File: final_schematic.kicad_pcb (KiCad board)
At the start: 2 copper layers, 0 parts

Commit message: Component Check Passed
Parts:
- added C1: 1uF, Capacitor_SMD:C_0603_1608Metric_Pad1.08x0.95mm_HandSolder, F.Cu at (-15.2, 27.3)
- added C10: 0.1uF, Capacitor_SMD:C_0402_1005Metric_Pad0.74x0.62mm_HandSolder, F.Cu at (-14.5, 115.2)
- added C11: 0.1uF, Capacitor_SMD:C_0402_1005Metric_Pad0.74x0.62mm_HandSolder, F.Cu at (-13.8, 125.4)
- added C12: 1uF, Capacitor_SMD:C_0603_1608Metric_Pad1.08x0.95mm_HandSolder, F.Cu at (-13.4, 135.0)
- added C13: 0.1uF, Capacitor_SMD:C_0402_1005Metric_Pad0.74x0.62mm_HandSolder, F.Cu at (-13.7, 145.2)
- added C14: 10uF, Capacitor_SMD:C_0603_1608Metric_Pad1.08x0.95mm_HandSolder, F.Cu at (-13.0, 155.1)
- added C15: 0.1uF, Capacitor_SMD:C_0402_1005Metric_Pad0.74x0.62mm_HandSolder, F.Cu at (-13.0, 164.9)
- added C16: 0.12uF, Capacitor_SMD:C_0603_1608Metric_Pad1.08x0.95mm_HandSolder, F.Cu at (-12.4, 175.1)
- added C17: 0.0068uF, Capacitor_SMD:C_0603_1608Metric_Pad1.08x0.95mm_HandSolder, F.Cu at (-11.4, 185.0)
- added C18: 0.1uF, Capacitor_SMD:C_0402_1005Metric_Pad0.74x0.62mm_HandSolder, F.Cu at (-12.9, 195.6)
- added C2: 1uF, Capacitor_SMD:C_0603_1608Metric_Pad1.08x0.95mm_HandSolder, F.Cu at (-15.3, 37.5)
- added C3: 1uF, Capacitor_SMD:C_0603_1608Metric_Pad1.08x0.95mm_HandSolder, F.Cu at (-15.4, 46.8)
- added C4: 1uF, Capacitor_SMD:C_0603_1608Metric_Pad1.08x0.95mm_HandSolder, F.Cu at (-15.2, 55.3)
- added C5: 0.1uF, Capacitor_SMD:C_0402_1005Metric_Pad0.74x0.62mm_HandSolder, F.Cu at (-15.3, 64.5)
- added C6: 0.1uF, Capacitor_SMD:C_0402_1005Metric_Pad0.74x0.62mm_HandSolder, F.Cu at (-15.2, 74.0)
- added C7: 0.1uF, Capacitor_SMD:C_0402_1005Metric_Pad0.74x0.62mm_HandSolder, F.Cu at (-15.1, 84.5)
- added C8: 0.1uF, Capacitor_SMD:C_0402_1005Metric_Pad0.74x0.62mm_HandSolder, F.Cu at (-14.9, 94.6)
- added C9: 0.1uF, Capacitor_SMD:C_0402_1005Metric_Pad0.74x0.62mm_HandSolder, F.Cu at (-14.7, 105.1)
- added D1: LED_HEARTBEAT_R1, Diode_SMD:D_0603_1608Metric_Pad1.05x0.95mm_HandSolder, F.Cu at (21.6, 16.5)
- added D2: LED_TRANSMIT_G1, Diode_SMD:D_0201_0603Metric_Pad0.64x0.40mm_HandSolder, F.Cu at (57.0, 17.2)
- added J1: BB_COM_Conn_01x04_Male, Connector_PinHeader_1.00mm:PinHeader_1x04_P1.00mm_Vertical, F.Cu at (113.6, 129.6)
- added J2: BB_CTRL_Conn_01x02_Male, Connector_PinHeader_1.00mm:PinHeader_1x02_P1.00mm_Vertical, F.Cu at (113.8, 151.0)
- added J3: BB_ON/OFF_Conn_01x04_Male, Connector_PinHeader_1.00mm:PinHeader_1x01_P1.00mm_Vertical, F.Cu at (112.3, 114.0)
- added J4: BOOT0_Conn_Male, Connector_PinHeader_1.00mm:PinHeader_1x01_P1.00mm_Vertical, F.Cu at (113.7, 144.8)
- added J5: OLED_SPI_Conn_01x04_Male, Connector_PinHeader_1.00mm:PinHeader_1x06_P1.00mm_Vertical, F.Cu at (112.5, 118.7)
- added J6: OLED_EN_Conn_01x02_Male, Connector_PinHeader_1.00mm:PinHeader_1x01_P1.00mm_Vertical, F.Cu at (113.4, 138.0)
- added J7: Conn_ARM_JTAG_SWD_10, Connector_PinHeader_1.27mm:PinHeader_2x05_P1.27mm_Vertical_SMD, F.Cu at (219.7, 68.6)
- added J8: GPS_COAX, Connector_Coaxial:U.FL_Molex_MCRF_73412-0110_Vertical, F.Cu at (240.0, 118.3)
- added LoRa_CON_Coaxial1: LoRa_Conn_Coaxial, Connector_Coaxial:U.FL_Molex_MCRF_73412-0110_Vertical, F.Cu at (244.0, 151.1)
- added R1: 48, Resistor_SMD:R_0603_1608Metric_Pad0.98x0.95mm_HandSolder, F.Cu at (-2.32, 39.5)
- added R10: 1k, Resistor_SMD:R_0402_1005Metric_Pad0.72x0.64mm_HandSolder, F.Cu at (-1.38, 106.3)
- added R2: 48, Resistor_SMD:R_0603_1608Metric_Pad0.98x0.95mm_HandSolder, F.Cu at (-2.32, 45.9)
- added R3: 10k, Resistor_SMD:R_0603_1608Metric_Pad0.98x0.95mm_HandSolder, F.Cu at (-2.45, 51.6)
- added R4: 10k, Resistor_SMD:R_0603_1608Metric_Pad0.98x0.95mm_HandSolder, F.Cu at (-2.50, 57.7)
- added R5: 10k, Resistor_SMD:R_0603_1608Metric_Pad0.98x0.95mm_HandSolder, F.Cu at (-2.51, 65.7)
- added R6: 510, Resistor_SMD:R_0603_1608Metric_Pad0.98x0.95mm_HandSolder, F.Cu at (-2.21, 73.5)
- added R7: 2.2k, Resistor_SMD:R_0603_1608Metric_Pad0.98x0.95mm_HandSolder, F.Cu at (-2.00, 81.1)
- added R8: 2.2k, Resistor_SMD:R_0603_1608Metric_Pad0.98x0.95mm_HandSolder, F.Cu at (-1.80, 89.3)
- added R9: 10k, Resistor_SMD:R_0603_1608Metric_Pad0.98x0.95mm_HandSolder, F.Cu at (-1.15, 101.0)
- added RED1: LED_GPS_R, Diode_SMD:D_0603_1608Metric_Pad1.05x0.95mm_HandSolder, F.Cu at (240.0, 110.2)
- added Re1: 10k, Resistor_SMD:R_0603_1608Metric_Pad0.98x0.95mm_HandSolder, F.Cu at (-2.19, 33.9)
- added Rf1: 10k, Resistor_SMD:R_0603_1608Metric_Pad0.98x0.95mm_HandSolder, F.Cu at (-2.41, 27.5)
- added S1: ON/OFF-SWITCH, Button_Switch_SMD:SW_SP3T_PCM13, F.Cu at (40.6, 160.0)
- added SW1: SW_Push_SESS, Button_Switch_SMD:SW_SPDT_CK-JS102011SAQN, F.Cu at (38.8, 17.8)
- added SW2: SW_Push_RADIO, Button_Switch_SMD:SW_SPST_PTS645, F.Cu at (163.2, 147.2)
- added SW3: SW_Push_RST, Button_Switch_SMD:SW_SPST_PTS645, F.Cu at (80.0, 149.9)
- added U1: STM32L476VGTx, Package_QFP:LQFP-100_14x14mm_P0.5mm, F.Cu at (166.4, 105.4)
- added U2: MTK3339, footprint_lib:FGPMMOPA6H, F.Cu at (223.5, 113.0)
- added U3: RFM95W-868S2, RF_Module:HOPERF_RFM9XW_SMD, F.Cu at (224.8, 144.8)
- added U4: BNO055, Package_LGA:LGA-28_5.2x3.8mm_P0.5mm, F.Cu at (218.4, 90.2)

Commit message: IMU, LORA, and GPS organized
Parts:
- moved C15 259.0 mm to (235.6, 92.1), turned to 90 degrees
- moved C16 256.6 mm to (230.4, 92.2), turned to 90 degrees
- moved C14 255.8 mm to (242.5, 144.0), turned to 180 degrees
- moved C17 254.3 mm to (225.3, 92.1), turned to 90 degrees
- moved C18 253.1 mm to (220.2, 97.0)
- moved Rf1 222.6 mm to (211.2, 90.1), turned to 90 degrees
- moved Re1 221.7 mm to (211.0, 94.7), turned to 90 degrees
- moved C13 220.2 mm to (203.1, 106.2), turned to 180 degrees
- moved R10 204.5 mm to (203.0, 112.3), turned to 180 degrees
- moved RED1 30.3 mm to (209.7, 112.3)
- moved LoRa_CON_Coaxial1 1.13 mm to (243.4, 150.2)

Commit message: Components spacialy assocsiated
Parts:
- moved C12 218.1 mm to (204.2, 149.3), turned to 180 degrees
- moved R9 211.5 mm to (206.1, 143.3), turned to 180 degrees
- moved C1 196.0 mm to (146.1, 138.7), turned to 180 degrees
- moved C2 176.2 mm to (129.6, 137.7)
- moved SW1 168.8 mm to (146.9, 147.5), turned to 0 degrees
- moved R3 168.7 mm to (142.0, 138.7)
- moved C3 159.3 mm to (115.5, 137.6)
- moved C6 158.9 mm to (141.6, 100.2)
- moved C7 157.9 mm to (141.6, 104.4)
- moved C8 157.1 mm to (141.6, 108.3)
- moved C9 156.5 mm to (141.6, 112.1)
- moved C10 156.1 mm to (141.6, 116.1)
- moved C11 155.5 mm to (141.6, 120.1)
- moved R7 155.4 mm to (152.2, 100.2)
- moved R8 154.7 mm to (152.8, 95.9)
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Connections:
- C15 pad 1: GND -> 3V3
- C15 pad 2: 3V3 -> GND
- J1 pad 1: I2C2_SDA -> GND
- J1 pad 2: I2C2_SCL -> V_supply
- J1 pad 3: V_supply -> I2C2_SDA
- J1 pad 4: GND -> I2C2_SCL

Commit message: Pre AI Routing Backup
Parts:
- moved D2 81.3 mm to (178.5, 133.1), turned to 90 degrees
- moved R2 68.6 mm to (177.6, 136.2), turned to 90 degrees
- moved C12 57.0 mm to (170.5, 103.3)
- moved R9 57.0 mm to (172.4, 97.3)
- moved J5 57.0 mm to (177.5, 93.7)
- moved J6 57.0 mm to (177.4, 103.2)
- moved J7 48.9 mm to (105.1, 91.5)
- moved J8 30.8 mm to (180.3, 120.8)
- moved U2 28.1 mm to (166.6, 115.5)
- moved R10 27.6 mm to (146.2, 116.5)
- moved RED1 27.6 mm to (152.9, 116.5)
- moved R8 22.9 mm to (130.2, 92.1)
- moved U1 22.9 mm to (133.2, 108.8)
- moved C13 22.9 mm to (150.9, 111.3)
- moved R7 22.9 mm to (129.6, 96.4)
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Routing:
- net GND: track 0.00 -> 122.6 mm
- net 3V3: track 0.00 -> 86.5 mm
- net NRST: track 0.00 -> 16.9 mm
- net PB0: track 0.00 -> 16.7 mm
- net V_supply: track 0.00 -> 14.6 mm
- net DIO0: track 0.00 -> 8.50 mm
- net Net-(LoRa_CON_Coaxial1-Pad1): track 0.00 -> 7.60 mm
- net Net-(J8-Pad1): track 0.00 -> 5.72 mm
- net Net-(D1-Pad1): track 0.00 -> 2.51 mm
- net Net-(D2-Pad1): track 0.00 -> 2.15 mm

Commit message: preperation for the robotic wars
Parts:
- moved J5 114.0 mm to (69.2, 58.3), turned to 90 degrees
- moved J6 108.4 mm to (78.7, 58.4), turned to 90 degrees
- moved R9 105.2 mm to (72.8, 63.4), turned to 270 degrees
- moved C12 99.3 mm to (78.8, 65.3), turned to 270 degrees
- moved RED1 71.4 mm to (94.0, 76.2)
- moved SW1 70.5 mm to (88.9, 104.1)
- moved U2 70.5 mm to (107.5, 77.0)
- moved C13 69.0 mm to (95.4, 70.3)
- moved C1 68.9 mm to (89.6, 95.9)
- moved R3 68.9 mm to (85.5, 95.9)
- moved J8 68.8 mm to (123.2, 82.3)
- moved U3 67.4 mm to (107.2, 96.3)
- moved D2 67.3 mm to (124.0, 93.7)
- moved C14 66.9 mm to (119.8, 95.3)
- moved C2 66.9 mm to (76.3, 94.7)
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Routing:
- net 3V3: track 86.5 -> 27.9 mm
- net GND: track 122.6 -> 155.9 mm
- net V_supply: track 14.6 -> 0.00 mm
- net Net-(J8-Pad1): track 5.72 -> 7.82 mm
- net Net-(LoRa_CON_Coaxial1-Pad1): track 7.60 -> 8.26 mm
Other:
- board outline added: 80.1 x 54.1 mm

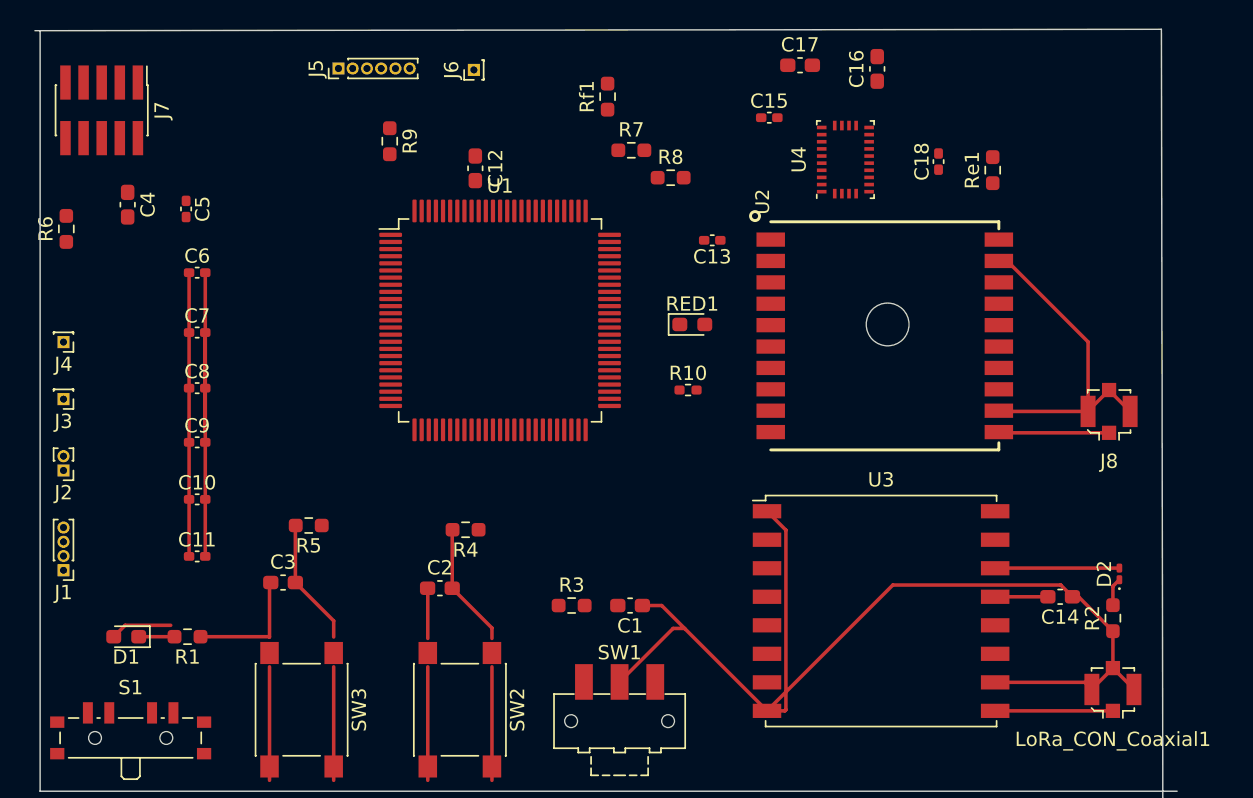
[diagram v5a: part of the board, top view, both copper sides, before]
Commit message: grounds and 3v3 mapped
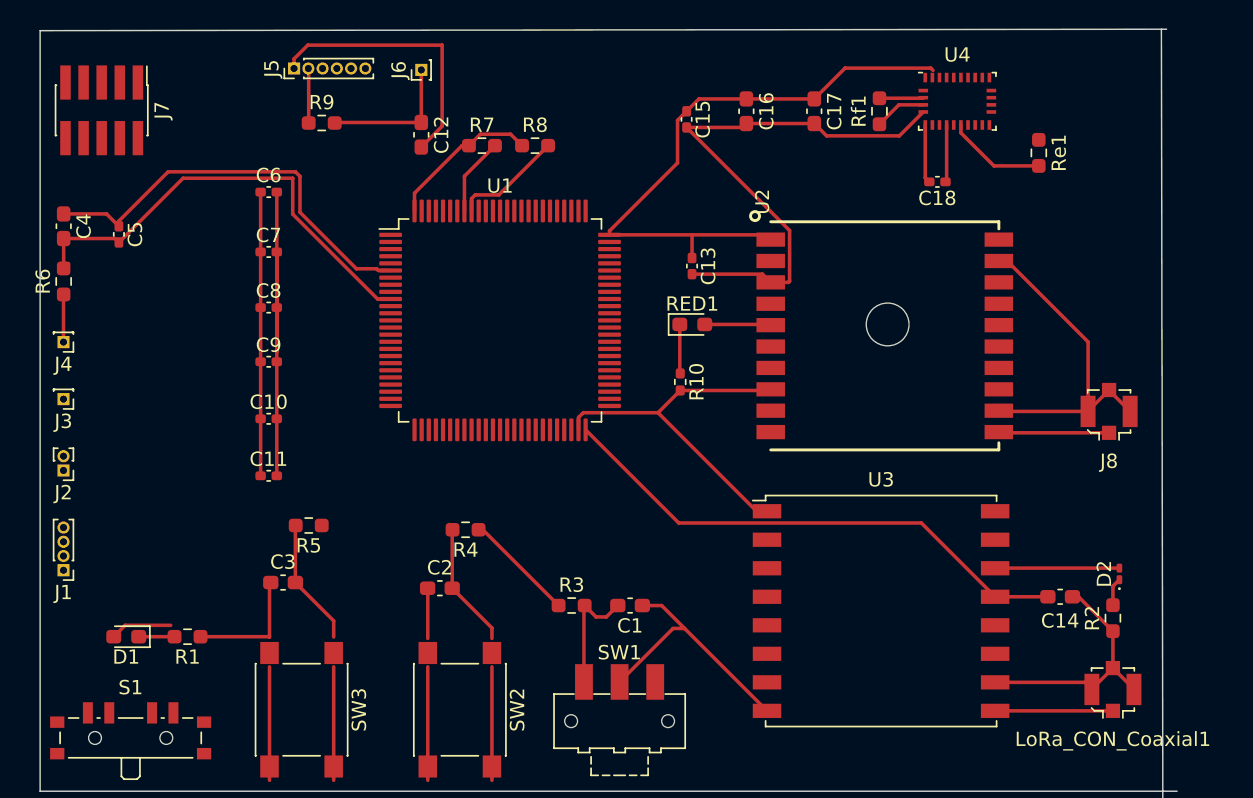
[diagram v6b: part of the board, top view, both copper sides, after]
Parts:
- moved Rf1 19.1 mm to (107.1, 61.3)
- moved R7 10.5 mm to (79.2, 63.7)
- moved R8 9.77 mm to (83.0, 63.7)
- moved C16 9.65 mm to (97.8, 61.3), turned to 270 degrees
- moved U4 8.85 mm to (112.6, 60.6), turned to 0 degrees
- moved C10 7.56 mm to (64.3, 82.8)
- moved C11 7.56 mm to (64.3, 86.8)
- moved C6 7.56 mm to (64.3, 66.9)
- moved C7 7.56 mm to (64.3, 71.1)
- moved C8 7.56 mm to (64.3, 75.0)
- moved C9 7.56 mm to (64.3, 78.8)
- moved C15 5.80 mm to (93.6, 61.8), turned to 270 degrees
- moved C5 5.04 mm to (53.8, 69.9)
- moved R9 4.94 mm to (68.0, 62.1), turned to 0 degrees
- moved C4 4.73 mm to (49.9, 69.3)
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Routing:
- net 3V3: track 27.9 -> 159.1 mm
- net GND: track 155.9 -> 235.8 mm
- net Net-(C12-Pad1): track 0.00 -> 9.77 mm
- net PB1: track 0.00 -> 8.37 mm
- net I2C_SCL: track 0.00 -> 7.77 mm
- net PE0: track 0.00 -> 6.98 mm
- net I2C_SDA: track 0.00 -> 5.47 mm
- net Net-(RED1-Pad2): track 0.00 -> 4.65 mm
- net Net-(C18-Pad1): track 0.00 -> 4.02 mm
- net Net-(Rf1-Pad1): track 0.00 -> 3.64 mm
- net Net-(R10-Pad1): track 0.00 -> 3.45 mm
- net BOOT0: track 0.00 -> 3.35 mm
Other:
- board size 80.1 x 54.1 mm -> 79.7 x 54.1 mm

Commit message: pcb checkpoint
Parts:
- removed J6: OLED_EN_Conn_01x02_Male, Connector_PinHeader_1.00mm:PinHeader_1x01_P1.00mm_Vertical
- removed J7: Conn_ARM_JTAG_SWD_10, Connector_PinHeader_1.27mm:PinHeader_2x05_P1.27mm_Vertical_SMD
- removed R7, R8: 2.2k, Resistor_SMD:R_0603_1608Metric_Pad0.98x0.95mm_HandSolder
- removed RED1: LED_GPS_R, Diode_SMD:D_0603_1608Metric_Pad1.05x0.95mm_HandSolder
- added R11: 62, Resistor_SMD:R_0603_1608Metric_Pad0.98x0.95mm_HandSolder, F.Cu at (124.7, 96.9)
- added U5: LT1129-3.3_SO8, Package_SO:SOIC-8_3.9x4.9mm_P1.27mm, F.Cu at (111.2, 81.1)
- C12: value 1uF -> 3.3uF; footprint Capacitor_SMD:C_0603_1608Metric_Pad1.08x0.95mm_HandSolder -> Capacitor_Tantalum_SMD:CP_EIA-7343-15_Kemet-W_Pad2.25x2.55mm_HandSolder
- J1: value BB_COM_Conn_01x04_Male -> Battery Babysitter; footprint Connector_PinHeader_1.00mm:PinHeader_1x04_P1.00mm_Vertical -> Connector_PinHeader_1.00mm:PinHeader_1x06_P1.00mm_Vertical
- J2: value BB_CTRL_Conn_01x02_Male -> BB_SYSOFF
- J3: value BB_ON/OFF_Conn_01x04_Male -> BOOT0; footprint Connector_PinHeader_1.00mm:PinHeader_1x01_P1.00mm_Vertical -> Connector_PinHeader_1.00mm:PinHeader_1x02_P1.00mm_Vertical
- J4: value BOOT0_Conn_Male -> OLED Qwiic; footprint Connector_PinHeader_1.00mm:PinHeader_1x01_P1.00mm_Vertical -> Connector_JST:JST_EH_S4B-EH_1x04_P2.50mm_Horizontal
- J5: value OLED_SPI_Conn_01x04_Male -> Programmer; footprint Connector_PinHeader_1.00mm:PinHeader_1x06_P1.00mm_Vertical -> Connector_PinHeader_1.00mm:PinHeader_1x04_P1.00mm_Vertical
- R1, R2: value 48 -> 62
- R10: value 1k -> 62; footprint Resistor_SMD:R_0402_1005Metric_Pad0.72x0.64mm_HandSolder -> Resistor_SMD:R_0603_1608Metric_Pad0.98x0.95mm_HandSolder
- R9: value 10k -> 62
- SW3: footprint Button_Switch_SMD:SW_SPST_PTS645 -> footprint_lib:SW_1825910-6-4
- moved R9 96.3 mm to (157.0, 98.8), turned to 180 degrees
- moved J2 82.4 mm to (132.3, 87.4), turned to 90 degrees
- moved C2 76.8 mm to (152.9, 99.7), turned to 90 degrees
- moved C15 73.0 mm to (166.3, 69.3), turned to 0 degrees
- moved C16 68.8 mm to (165.8, 71.9), turned to 180 degrees
- moved SW2 66.7 mm to (144.3, 101.4), turned to 0 degrees
- moved C17 64.6 mm to (165.7, 74.9), turned to 180 degrees
- moved C3 63.6 mm to (128.9, 96.9), turned to 180 degrees
- moved SW3 63.4 mm to (130.0, 101.4), turned to 0 degrees
- moved R5 61.7 mm to (128.8, 92.7)
- moved R4 59.5 mm to (137.0, 98.8), turned to 0 degrees
- moved J4 56.2 mm to (105.9, 72.2), turned to 90 degrees
- moved Rf1 52.6 mm to (159.4, 67.9)
- moved J3 51.8 mm to (64.8, 31.9), turned to 0 degrees
- moved S1 50.0 mm to (104.6, 102.7)
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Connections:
- C1 pad 2: PB1 -> Net-(C1-Pad2)
- C12 pad 1: Net-(C12-Pad1) -> 3V3
- C15 pad 1: 3V3 -> GND
- C15 pad 2: GND -> 3V3
- C2 pad 2: PB0 -> Net-(C2-Pad2)
- C3 pad 2: NRST -> Net-(C3-Pad2)
- J1 pad 3: I2C2_SDA -> I2C3_SDA
- J1 pad 4: I2C2_SCL -> I2C3_SCL
- J2 pad 1: PB12 -> GND
- J2 pad 2: PB13 -> SYSOFF
- J3 pad 1: PB14 -> BOOT0
- J4 pad 1: BOOT0 -> GND
- J5 pad 3: SPI1_MOSI -> SWDIO
- J5 pad 4: SPI1_SCK -> SWCLK
- R10 pad 1: Net-(R10-Pad1) -> session_btn
- R10 pad 2: GND -> Net-(C1-Pad2)
- R3 pad 2: PB1 -> Net-(C1-Pad2)
- R4 pad 2: PB0 -> Net-(C2-Pad2)
- R5 pad 2: NRST -> Net-(C3-Pad2)
- R9 pad 1: 3V3 -> radio_btn
- R9 pad 2: Net-(C12-Pad1) -> Net-(C2-Pad2)
- Re1 pad 2: PE0 -> IMU_nRST
- S1 pad 2: 3V3 -> BB_Out
- SW1 pad 1: PB1 -> Net-(C1-Pad2)
- SW2 pad 1: PB0 -> Net-(C2-Pad2)
- SW3 pad 1: NRST -> Net-(C3-Pad2)
- U1 pad 1: Net-(U1-Pad1) -> session_btn
- U1 pad 12: PH0 -> Net-(U1-Pad12)
- U1 pad 13: PH1 -> Net-(U1-Pad13)
- U1 pad 15: Net-(U1-Pad15) -> I2C3_SCL
- U1 pad 16: Net-(U1-Pad16) -> I2C3_SDA
- U1 pad 17: Net-(U1-Pad17) -> BB_CE
- U1 pad 18: Net-(U1-Pad18) -> BB_GPOUT
- U1 pad 2: PE3 -> radio_btn
- U1 pad 23: Net-(U1-Pad23) -> SYSOFF
- U1 pad 26: PA3 -> Net-(U1-Pad26)
- U1 pad 29: CS_OLED -> Net-(U1-Pad29)
- U1 pad 33: Net-(U1-Pad33) -> LoRa_RST
- U1 pad 34: Net-(U1-Pad34) -> CS_LORA
- U1 pad 35: PB0 -> Net-(U1-Pad35)
- U1 pad 36: PB1 -> Net-(U1-Pad36)
- U1 pad 43: CS_LORA -> IMU_ADDR
- U1 pad 44: Net-(U1-Pad44) -> BL_IND
- U1 pad 45: Net-(U1-Pad45) -> IMU_INT
- U1 pad 46: Net-(U1-Pad46) -> IMU_nRST
- U1 pad 51: PB12 -> Net-(U1-Pad51)
- U1 pad 52: PB13 -> Net-(U1-Pad52)
- U1 pad 53: PB14 -> Net-(U1-Pad53)
- U1 pad 67: DC_OLED -> Net-(U1-Pad67)
- U1 pad 68: Net-(U1-Pad68) -> USART_TX
- U1 pad 69: Net-(U1-Pad69) -> USART_RX
- U1 pad 85: USART_TX -> Net-(U1-Pad85)
- U1 pad 86: USART_RX -> Net-(U1-Pad86)
- U1 pad 89: SWO -> Net-(U1-Pad89)
- U1 pad 92: I2C_SCL -> I2C1_SCL
- U1 pad 93: I2C_SDA -> I2C1_SDA
- U1 pad 97: PE0 -> Net-(U1-Pad97)
- U2 pad 9: USART_RX -> N-00000104
- U3 pad 6: PA3 -> LoRa_RST
- U4 pad 10: PH1 -> BL_IND
- U4 pad 11: PE0 -> IMU_nRST
- U4 pad 14: PE3 -> IMU_INT
- U4 pad 17: PH0 -> IMU_ADDR
- U4 pad 19: I2C_SCL -> I2C2_SCL
- U4 pad 20: I2C_SDA -> I2C2_SDA
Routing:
- net GND: track 235.8 -> 0.00 mm
- net 3V3: track 159.1 -> 0.00 mm
- net NRST: track 16.9 -> 0.00 mm
- net PB0: track 16.7 -> 0.00 mm
- net Net-(C12-Pad1): track 9.77 -> 0.00 mm
- net DIO0: track 8.73 -> 0.00 mm
- net PB1: track 8.37 -> 0.00 mm
- net Net-(LoRa_CON_Coaxial1-Pad1): track 8.26 -> 0.00 mm
- net Net-(J8-Pad1): track 7.82 -> 0.00 mm
- net I2C_SCL: track 7.77 -> 0.00 mm
- net PE0: track 6.98 -> 0.00 mm
- net I2C_SDA: track 5.47 -> 0.00 mm
- net Net-(U2-Pad5): track 4.65 -> 0.00 mm
- net Net-(C18-Pad1): track 4.02 -> 0.00 mm
- net Net-(Rf1-Pad1): track 3.64 -> 0.00 mm
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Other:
- board outline removed
